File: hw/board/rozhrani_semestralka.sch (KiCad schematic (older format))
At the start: 56 parts, among them P1 DISPLAY_CONN, P2 DISPLAY_VCC_CON, P3 USB_B, U1 MCP2210, U2 MIC5504-3.3, U3 Joystick, U4 LM239, U5 CD4532, U6 NPIC6c596, U7 NE555, U8 BS800N, U9 BS800N

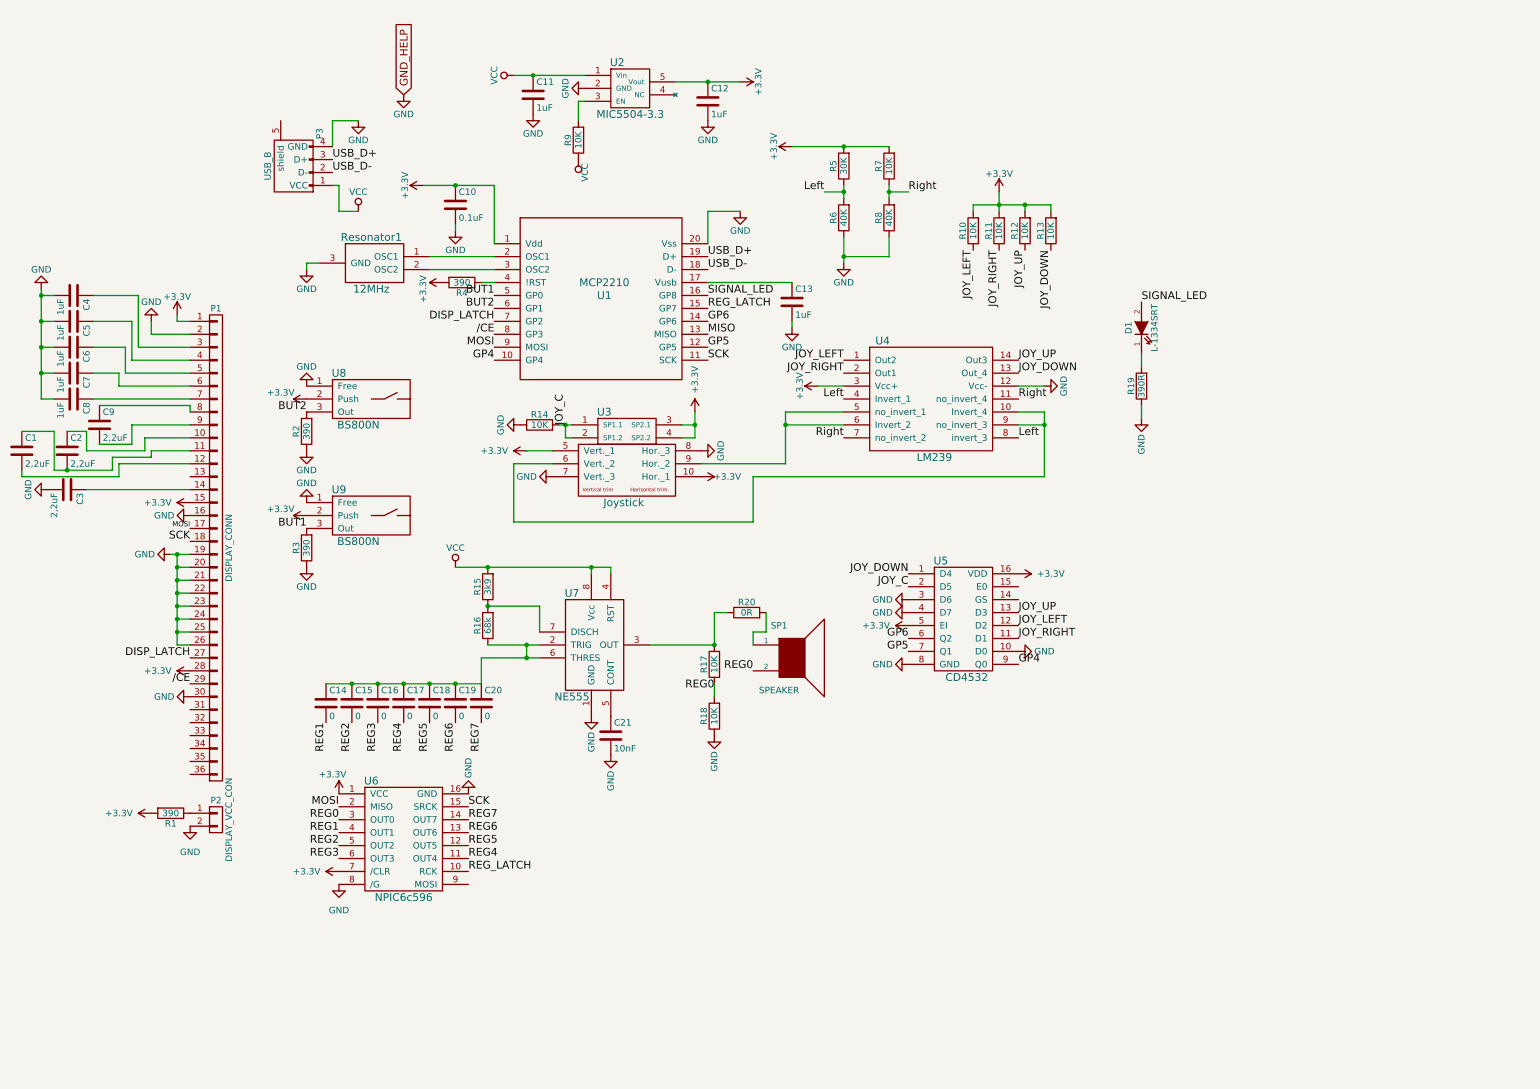
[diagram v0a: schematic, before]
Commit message: Upgrade value of resitors neer to joystick + added bom
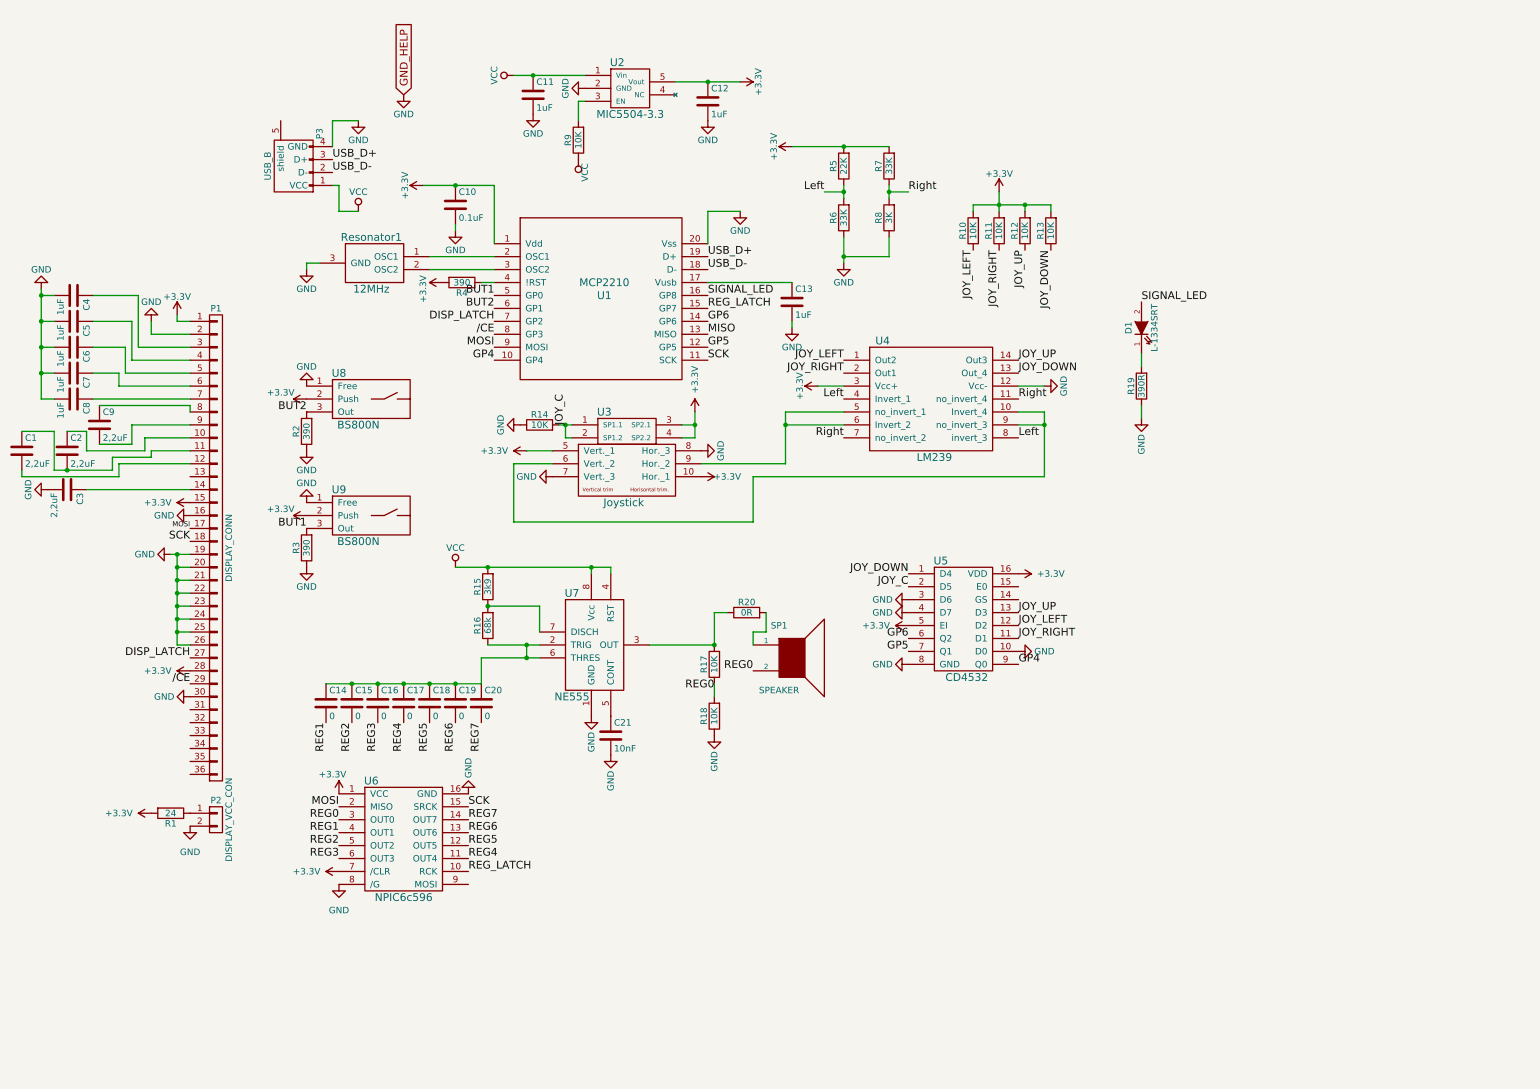
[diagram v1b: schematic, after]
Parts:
- R1: value 390 -> 24
- R5: value 30K -> 22K
- R6: value 40K -> 33K
- R7: value 10K -> 33K
- R8: value 40K -> 3K
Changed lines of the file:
@@
 P 7250 1450
 F 0 "R5" V 7330 1450 50  0000 C CNN
-F 1 "30K" V 7250 1450 50  0000 C CNN
+F 1 "22K" V 7250 1450 50  0000 C CNN
 F 2 "Resistors_SMD:R_0603_HandSoldering" V 7180 1450 30  0001 C CNN
 F 3 "" H 7250 1450 30  0000 C CNN
@@
 P 7250 1850
 F 0 "R6" V 7330 1850 50  0000 C CNN
-F 1 "40K" V 7250 1850 50  0000 C CNN
+F 1 "33K" V 7250 1850 50  0000 C CNN
 F 2 "Resistors_SMD:R_0603_HandSoldering" V 7180 1850 30  0001 C CNN
 F 3 "" H 7250 1850 30  0000 C CNN
@@
 P 7600 1450
 F 0 "R7" V 7680 1450 50  0000 C CNN
-F 1 "10K" V 7600 1450 50  0000 C CNN
+F 1 "33K" V 7600 1450 50  0000 C CNN
 F 2 "Resistors_SMD:R_0603_HandSoldering" V 7530 1450 30  0001 C CNN
 F 3 "" H 7600 1450 30  0000 C CNN
@@
 P 7600 1850
 F 0 "R8" V 7680 1850 50  0000 C CNN
-F 1 "40K" V 7600 1850 50  0000 C CNN
+F 1 "3K" V 7600 1850 50  0000 C CNN
 F 2 "Resistors_SMD:R_0603_HandSoldering" V 7530 1850 30  0001 C CNN
 F 3 "" H 7600 1850 30  0000 C CNN
@@
 P 2050 6450
 F 0 "R1" V 2130 6450 50  0000 C CNN
-F 1 "390" V 2050 6450 50  0000 C CNN
+F 1 "24" V 2050 6450 50  0000 C CNN
 F 2 "Resistors_SMD:R_0603_HandSoldering" V 1980 6450 30  0001 C CNN
 F 3 "" H 2050 6450 30  0000 C CNN

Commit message: Sorting schematic parts
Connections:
- net JOY_C: no longer R14.2, U3.1 (SP1.1), U3.2 (SP1.2)
- new net: R14.2, U3.1 (SP1.1), U3.2 (SP1.2)
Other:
- moved on the sheet: C1, C10, C11, C12, C13, C14, C15, C16, C17, C18, C19, C2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

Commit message: just updated schematic package in NPIC6C596
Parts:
- removed U6: NPIC6c596, Housings_SOIC:SOIC-16_3.9x9.9mm_Pitch1.27mm, symbol TIPC6C595
- added U6: NPIC6C596, symbol NPIC6C596
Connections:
- net +3V3: now also U6.1 (VCC), U6.7 (/CLR)
- net GND: now also U6.16 (GND), U6.8 (/G)
- net MOSI: now also U6.2 (Data_in)
- net REG0: now also U6.3 (OUT0)
- net REG1: now also U6.4 (OUT1)
- net REG2: now also U6.5 (OUT2)
- net REG3: now also U6.6 (OUT3)
- net REG4: now also U6.11 (OUT4)
- net REG5: now also U6.12 (OUT5)
- net REG6: now also U6.13 (OUT6)
- net REG7: now also U6.14 (OUT7)
- net REG_LATCH: now also U6.10 (RCK)
- net SCK: now also U6.15 (SRCK)

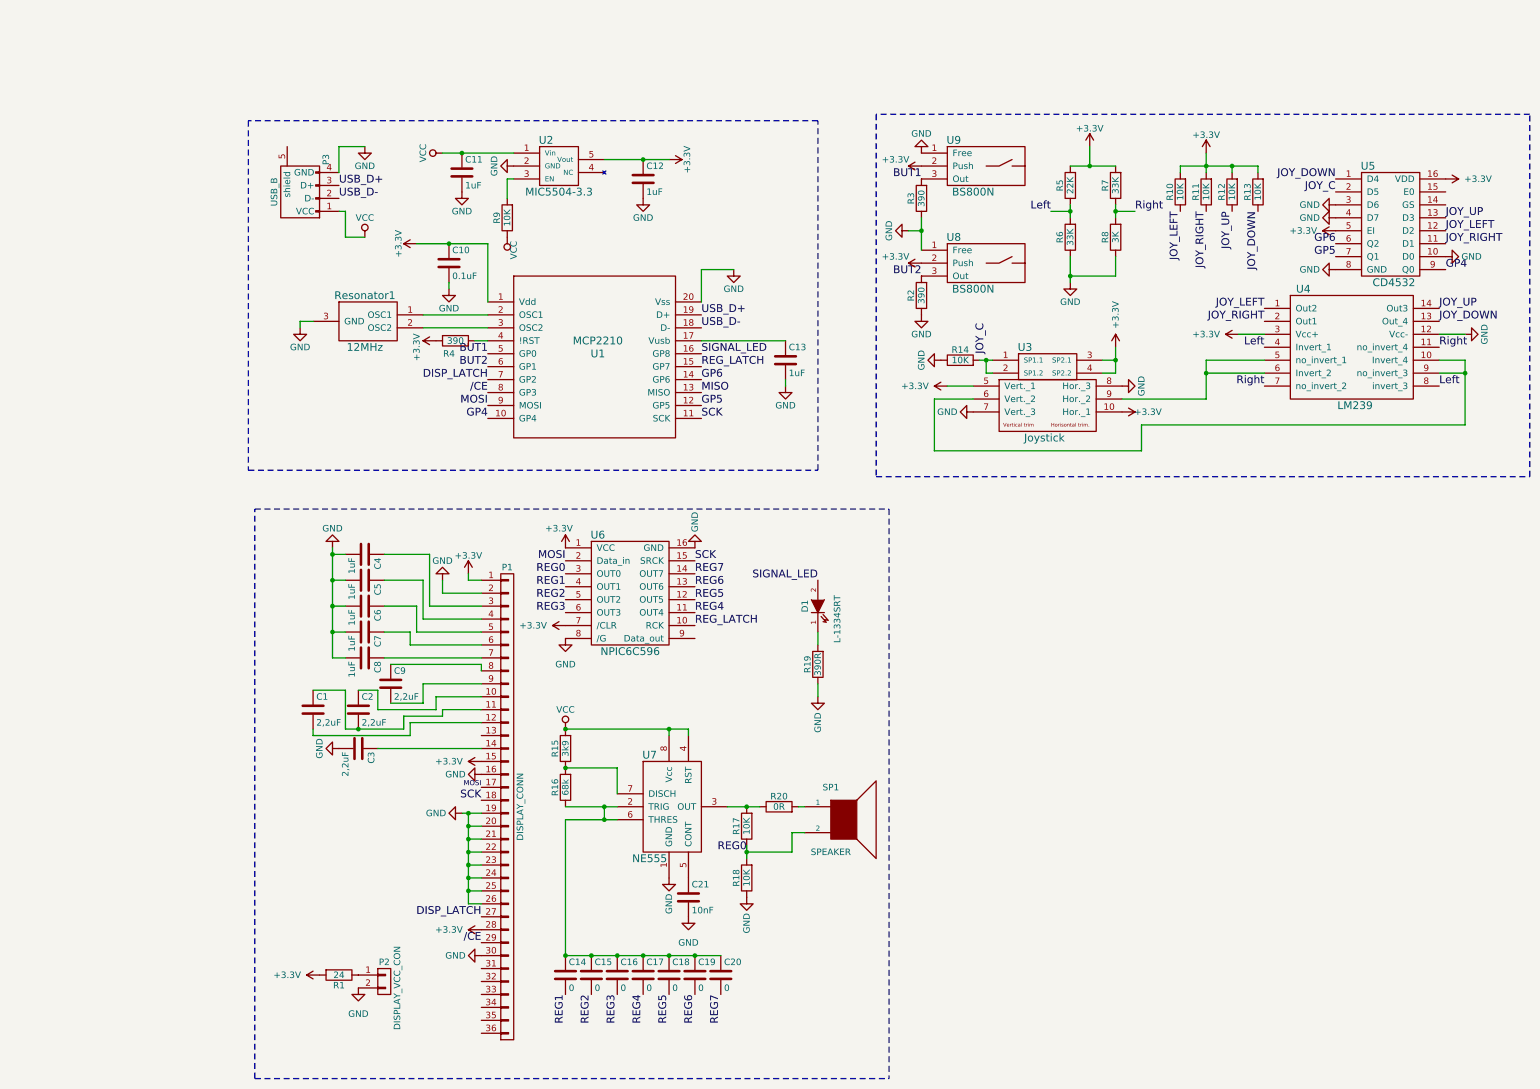
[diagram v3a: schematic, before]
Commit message: Added hw board version 1.0.0 - buttons to another side and small updates
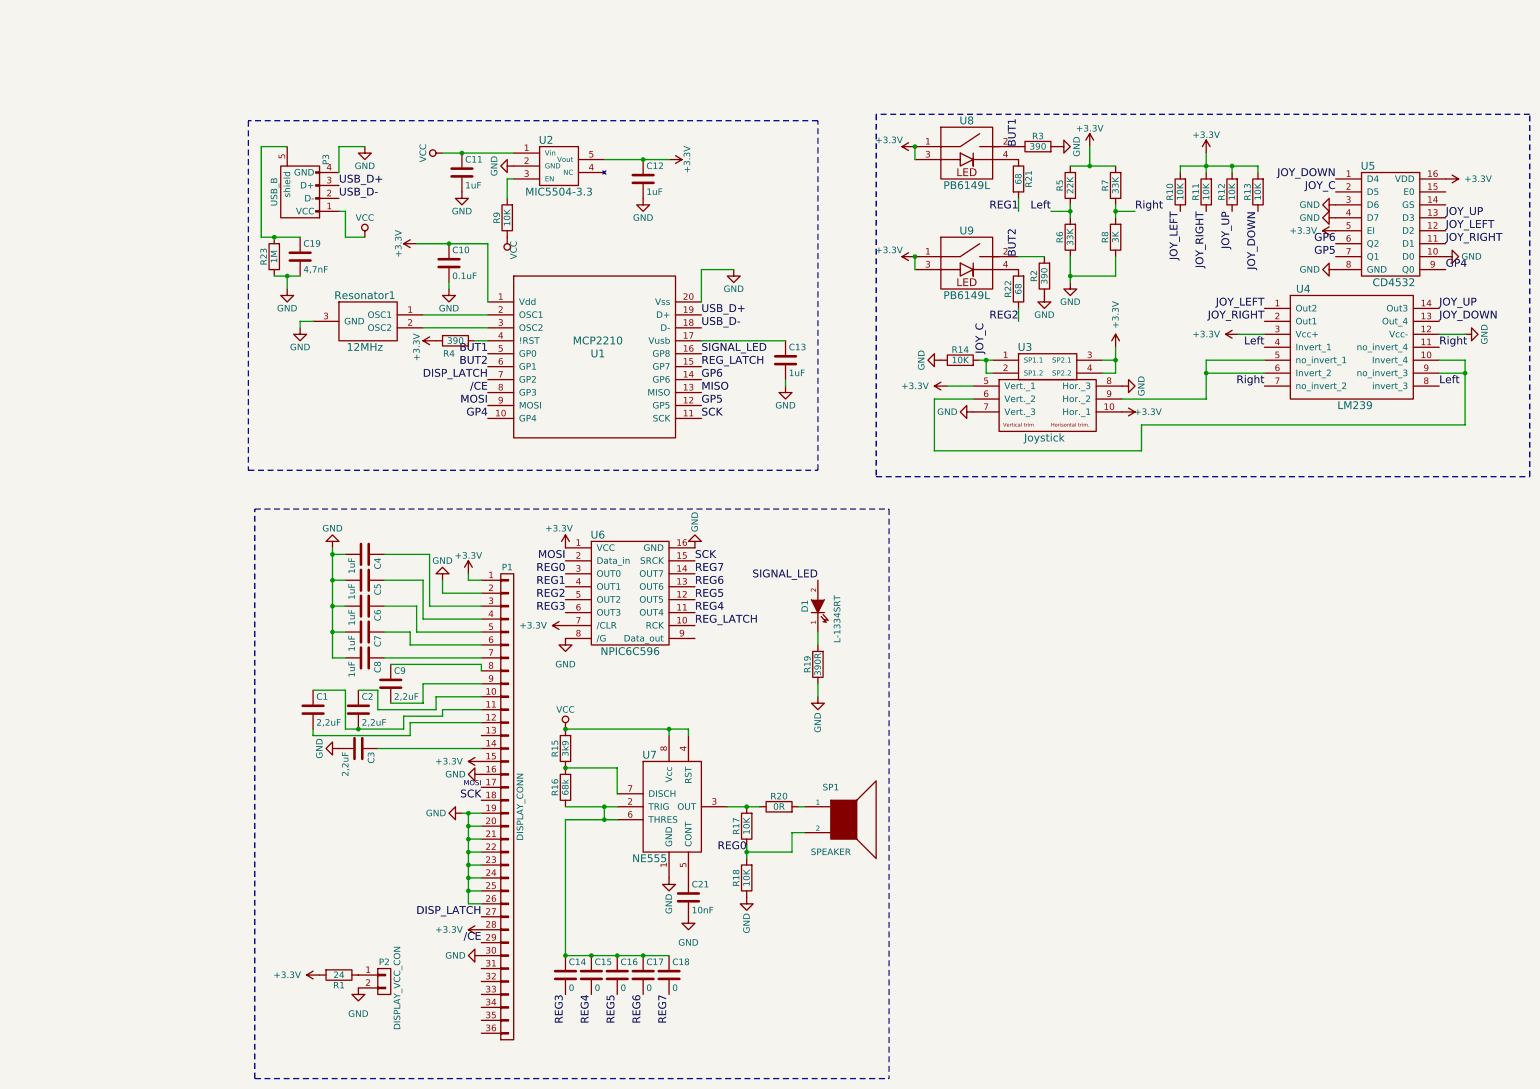
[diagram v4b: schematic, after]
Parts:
- removed C20: 0, Capacitors_SMD:C_0603_HandSoldering, symbol C
- removed U8, U9: BS800N, pcb:BS-800-N, symbol BS800N
- added R21, R22: 68, Resistors_SMD:R_0603_HandSoldering, symbol R
- added R23: 1M, Resistors_SMD:R_0603_HandSoldering, symbol R
- added U8, U9: PB6149L, pcb:PB6149L, symbol PB6149L
- C19: value 0 -> 4,7nF
- SP1: footprint pcb:buzer -> pcb:Buzzer
- U6: footprint (none) -> Housings_SOIC:SOIC-16_3.9x9.9mm_Pitch1.27mm
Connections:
- net +3V3: now also U8.1, U8.3, U9.1, U9.3
- net BUT1: now also R3.1, U8.2; no longer R3.2
- net BUT2: now also U9.2
- net GND: now also C19.2, R3.2, R23.1; no longer R3.1
- net REG1: now also R21.2; no longer C14.2
- net REG2: now also R22.1; no longer C15.2
- net REG3: now also C14.2; no longer C16.2
- net REG4: now also C15.2; no longer C17.2
- net REG5: now also C16.2; no longer C18.2
- net REG6: now also C17.2; no longer C19.2
- net REG7: now also C18.2
- net at P3.5 (shield): now also C19.1, R23.2
- net at C14.1, C15.1, C16.1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: no longer C19.1
- new net: R21.1, U8.4
- new net: R22.2, U9.4
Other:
- moved on the sheet: R2, R3
